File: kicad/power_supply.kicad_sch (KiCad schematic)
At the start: 29 parts, among them T1 reuse / AnTek AS-0524, U1 LM317T

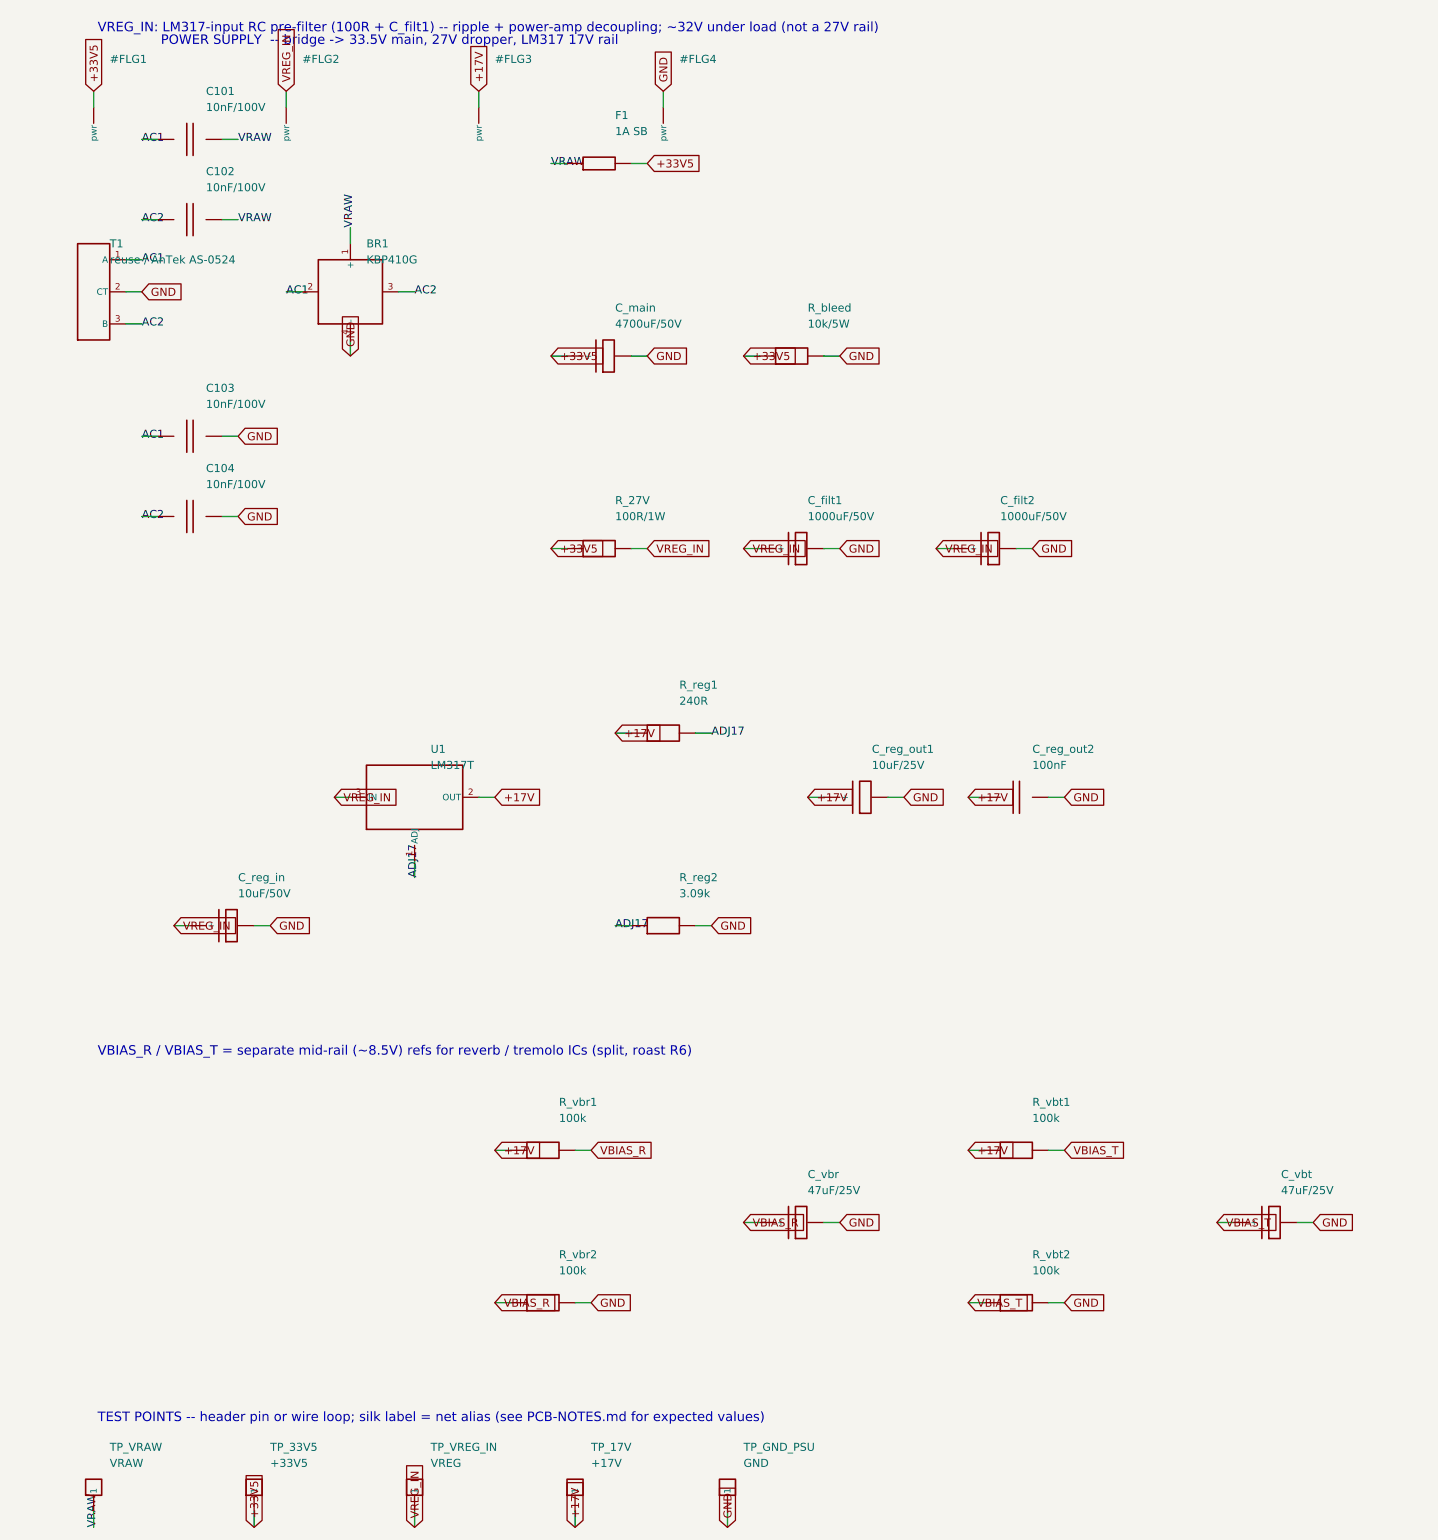
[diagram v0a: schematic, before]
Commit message: Noise, hum, crosstalk and thermal models; three design fixes; JLCPCB rules and cost
New models (docs/06c, spice/): a .noise run of the whole front end including the
LM317's own rail noise, the rail-ripple paths to the speaker, a vactrol-level tremolo
depth model, an electro-thermal LM1875 ladder, and a geometric crosstalk audit of the
routed boards (kicad/gen/crosstalk_audit.py). They found three defects:

- Errata #21 (hum + hiss): the LM1875 bias divider had no bypass (+4 dB ripple to
  speaker, 0.4 Vrms of 100 Hz at idle) and the LM317's 0.5 mV of noise reached the
  0 dB-PSRR JFET stages (23 dB above their floor, SNR 34 dB). Fixed with C_bref +
  R_bias3 on the power amp, C_adj on the regulator, and an RC-decoupled +17V_PRE rail
  for Q1/Q2/Q_rec: hum 408 mV -> 0.3 mV, EIN 37 -> 2.7 uV, SNR 34 -> 57 dB.
- Errata #22 (tremolo depth 1.7 dB): the vactrol LED was returned to ground from a
  mid-rail LFO -> 7 mA DC, a fixed -20 dB pad. LED limiter (2 V swing, LED_rate is one
  limiter LED) + Q_trem 2N3904/MMBT3904 emitter follower AC-coupled from the depth
  pot -> 15 dB depth, 0.8 dB insertion loss.
- Errata #23 (fab): stock TO-92 and the LM1875 footprint were under JLCPCB's 0.18 mm
  annular-ring minimum -> TO-92_Inline_Wide and 1.5 mm LM1875 pads; both .kicad_pro
  carry JLC's 2-layer limits as DRC constraints. Cost: all SMD caps 1206 (basic
  library), "(opt)" MRB caps DNP, gyrator on E24 values (same 1.86 H): 7 -> 2
  extended part types, ~$32 -> ~$17 assembly for five boards (kicad/gen/jlc_cost.py);
  three fiducials on the SMD board.

Crosstalk -> two routing rules (.kicad_dru: HighCurrent 0.6/0.4 mm and TankDrive
1.2/0.8 mm from signal copper, THT/SMD) that route_board.py also hands the router as
class clearances; keepout rule areas along the edge and around the mounting holes.
Thermal: Part 5's <= 2.5 K/W heatsink confirmed with numbers (Tj 97 C at 40 C ambient,
worst-case sine; 8-10 K/W clip-ons reach shutdown).

Placer: short parts stack beside tall ones i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
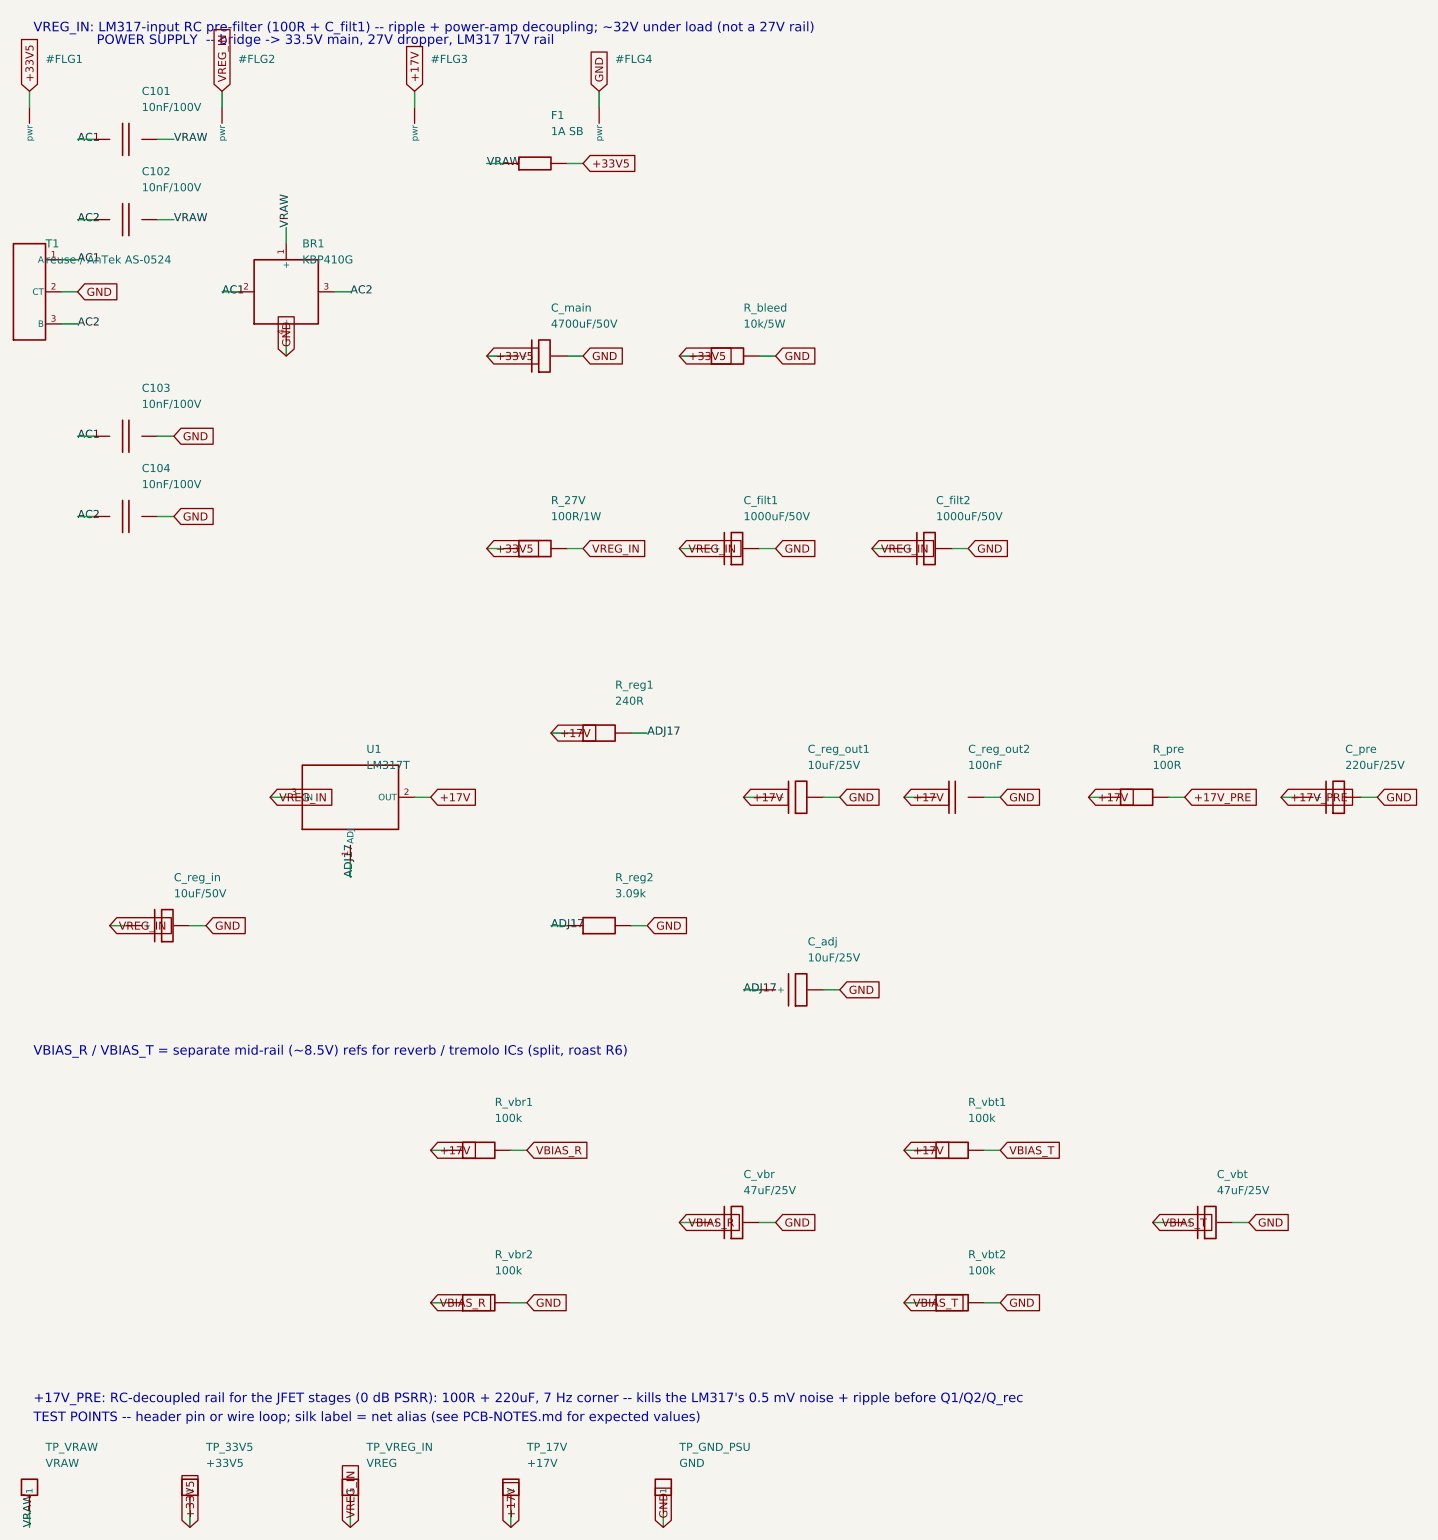
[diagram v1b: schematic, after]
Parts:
- added C_adj: 10uF/25V, Capacitor_THT:CP_Radial_D5.0mm_P2.00mm, symbol cr_primitives:CP
- added C_pre: 220uF/25V, Capacitor_THT:CP_Radial_D6.3mm_P2.50mm, symbol cr_primitives:CP
- added R_pre: 100R, Resistor_THT:R_Axial_DIN0207_L6.3mm_D2.5mm_P5.08mm_Vertical, symbol cr_primitives:R
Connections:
- net +17V: now also R_pre.1
- net ADJ17: now also C_adj.1 (+)
- net GND: now also C_adj.2, C_pre.2
- new net +17V_PRE: C_pre.1 (+), R_pre.2
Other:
- note added: "+17V_PRE: RC-decoupled rail for the JFET stages (0 dB PSRR): 100R + 220uF, 7 Hz corner -- kills the LM317's 0.5 mV noise + ripple before Q1/Q2/Q_rec"
